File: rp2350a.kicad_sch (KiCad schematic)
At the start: 48 parts, among them Q7 DMN1150UFB-7B, U32 RP2354A, U34 TS2306A 240GF MSM 9_C2976675, U9 TXU0101DCKR, X3 OT4EL89CJI-111YLC-12M

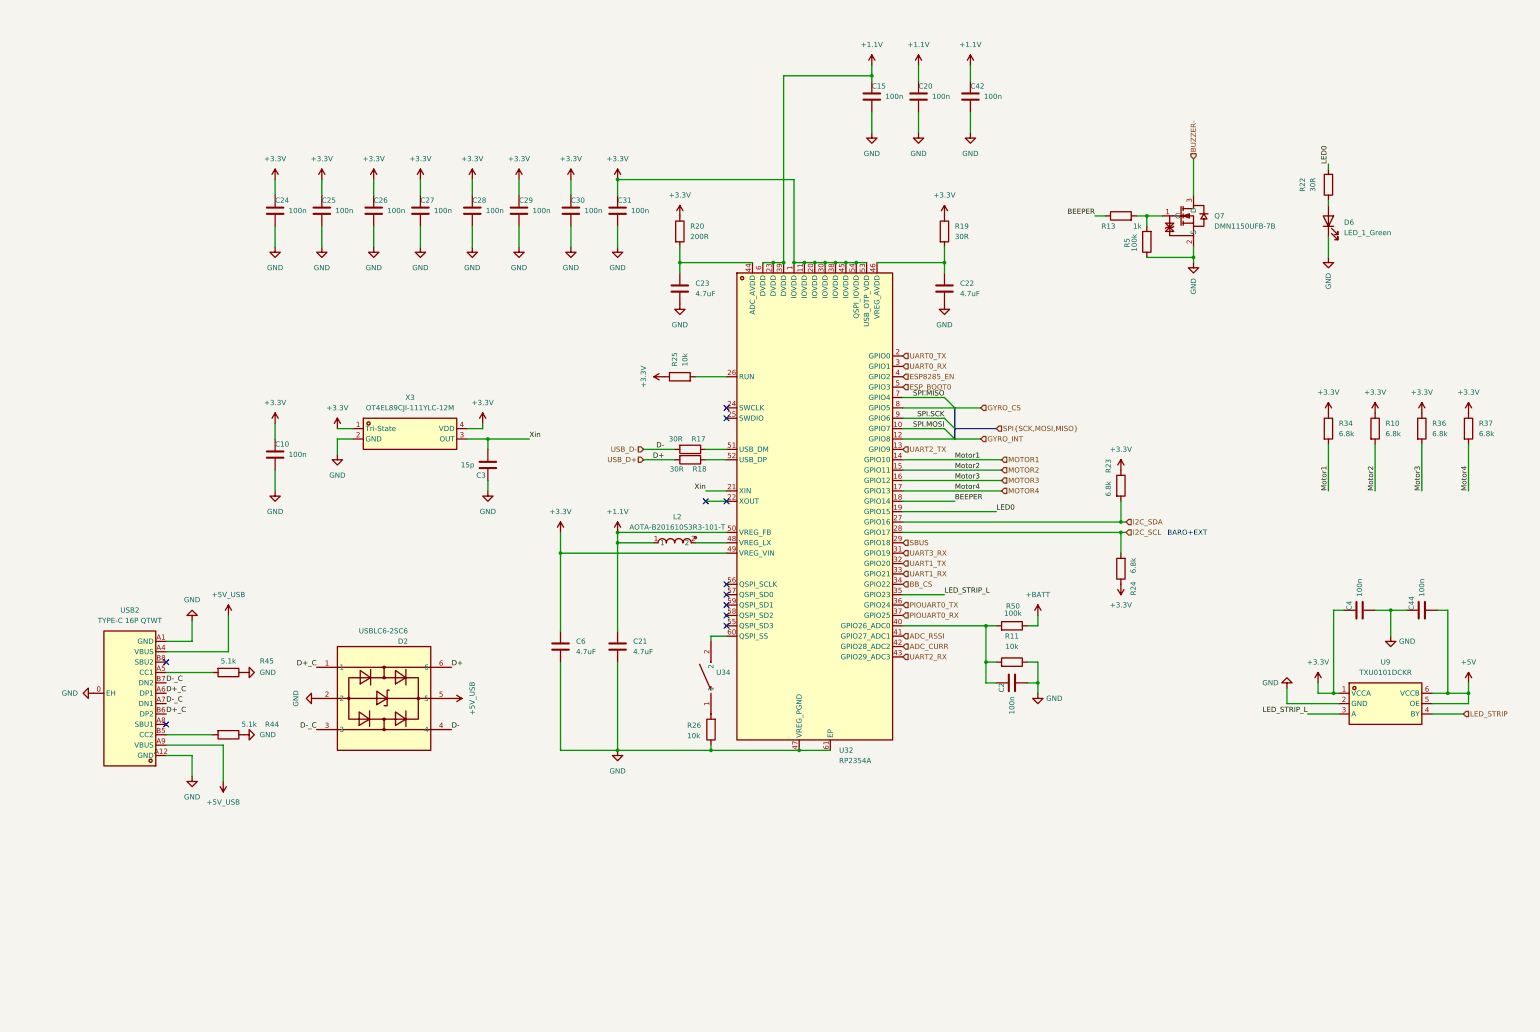
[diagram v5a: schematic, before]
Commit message: Switched to RP2354B for V2 of the FC for more IO. I want to try implement OSD on PIO state machine. I know BF already uses all of them but it should be possible and then later try to combine it witht the WS2812 protocol PIO2. If anybody here has any experience with analog OSD generation let me know, I just want to make a circuit that would allow further software development later. The reason I want to do it this way is it's cheap BOM<1 euro and low footprint, just 2 2x2 IC's and some passives.
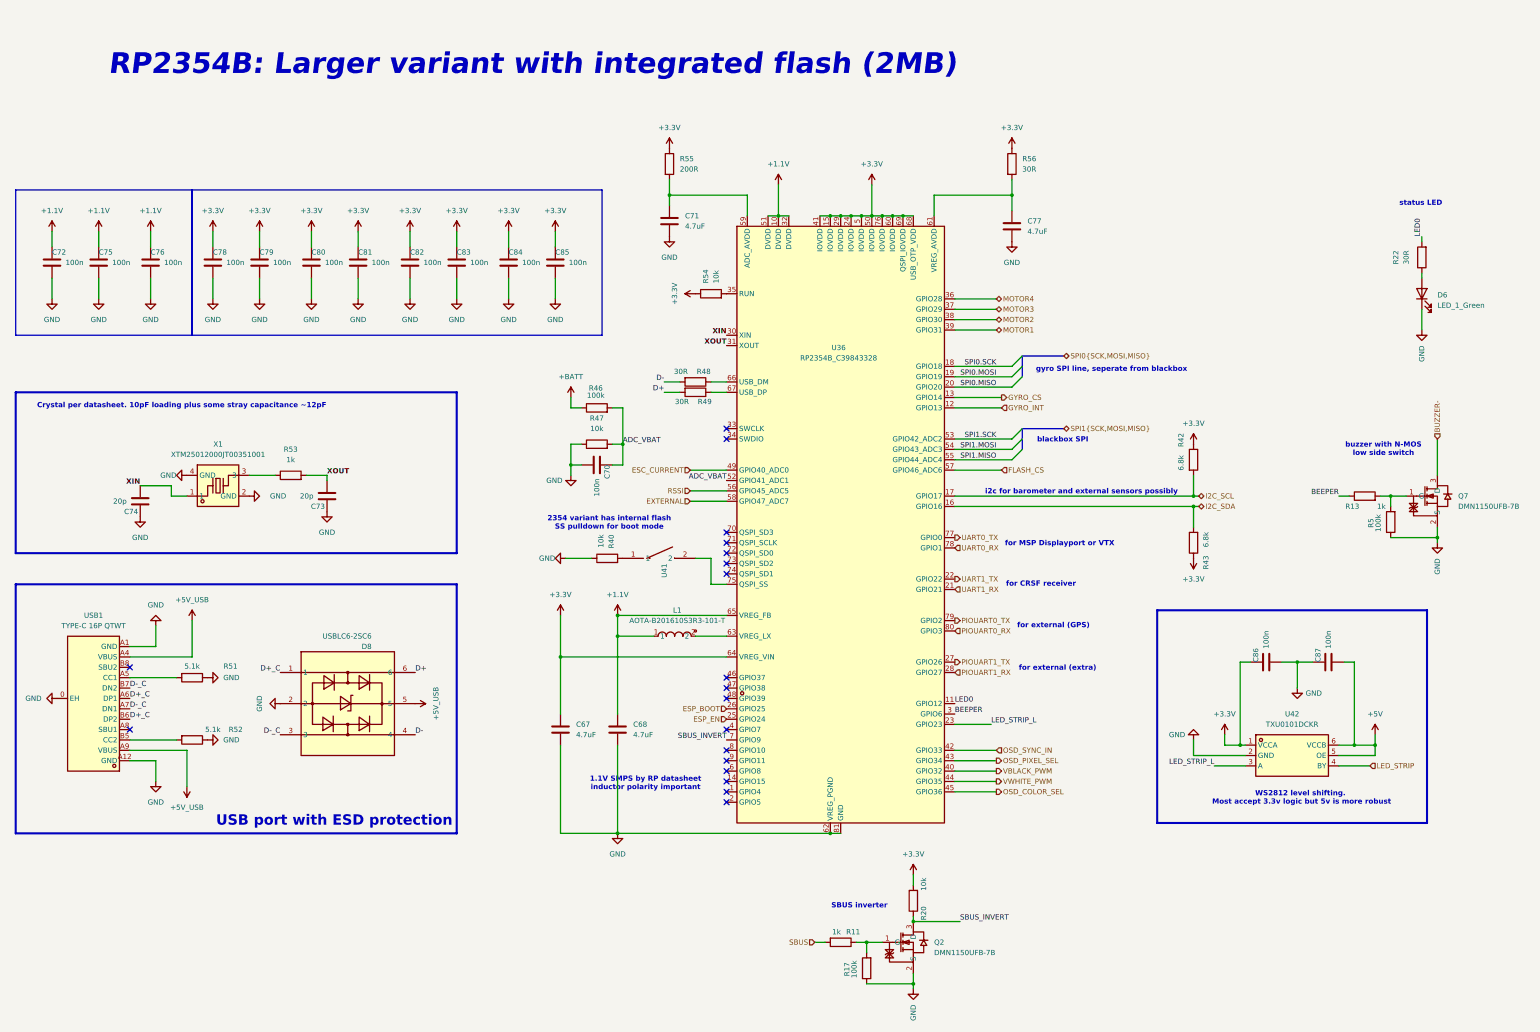
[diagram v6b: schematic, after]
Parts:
- removed C10, C15, C2, C20, C24, C25, C26, C27, C28, C29, C30, C31, C4, C42, C44: 100n, Capacitor_SMD:C_0402_1005Metric, symbol Device:C
- removed C21, C22, C23, C6: 4.7uF, Capacitor_SMD:C_0402_1005Metric, symbol Device:C
- removed C3: 15p, Capacitor_SMD:C_0402_1005Metric, symbol Device:C
- removed D2: USBLC6-2SC6, lib:SOT-23-6_L2.9-W1.6-P0.95-LS2.8-BL, symbol lib:USBLC6-2SC6
- removed L2: AOTA-B201610S3R3-101-T, lib:IND-SMD_L2.0-W1.6_AOTA-B201610S3R3-101-T, symbol lib:AOTA-B201610S3R3-101-T
- removed R10, R23, R24, R34, R36, R37: 6.8k, Resistor_SMD:R_0402_1005Metric, symbol Device:R
- removed R18, R19: 30R, Resistor_SMD:R_0402_1005Metric, symbol Device:R
- removed R25, R26: 10k, Resistor_SMD:R_0402_1005Metric, symbol Device:R
- removed R44, R45: 5.1k, Resistor_SMD:R_0402_1005Metric, symbol Device:R
- removed R50: 100k, Resistor_SMD:R_0402_1005Metric, symbol Device:R
- removed U32: RP2354A, lib:QFN-60_L7.0-W7.0-P0.40-TL-EP3.4, symbol lib:RP2354A
- removed U34: TS2306A 240GF MSM 9_C2976675, lib:SW-SMD_4P-L3.0-W2.0-P0.85-LS3.5, symbol lib:TS2306A240GFMSM9_C2976675
- removed U9: TXU0101DCKR, lib:SC-70-6_L2.0-W1.3-P0.65-LS2.1-BL, symbol lib:TXU0101DCKR
- removed USB2: TYPE-C 16P QTWT, lib:USB-TYPE-C-SMD_TYPE-C-16P-QTWT, symbol lib:TYPE-C16PQTWT
- removed X3: OT4EL89CJI-111YLC-12M, lib:OSC-SMD_4P-L1.6-W1.2-BL-1, symbol lib:OT4EL89CJI-111YLC-12M
- added C67, C68, C71, C77: 4.7uF, Capacitor_SMD:C_0402_1005Metric, symbol Device:C
- added C70, C72, C75, C76, C78, C79, C80, C81, C82, C83, C84, C85, C86, C87: 100n, Capacitor_SMD:C_0402_1005Metric, symbol Device:C
- added C73, C74: 20p, Capacitor_SMD:C_0402_1005Metric, symbol Device:C
- added D8: USBLC6-2SC6, lib:SOT-23-6_L2.9-W1.6-P0.95-LS2.8-BL, symbol lib:USBLC6-2SC6
- added L1: AOTA-B201610S3R3-101-T, lib:IND-SMD_L2.0-W1.6_AOTA-B201610S3R3-101-T, symbol lib:AOTA-B201610S3R3-101-T
- added Q2: DMN1150UFB-7B, lib:DFN-3L_L1.0-W0.6-P0.65-BR, symbol lib:DMN1150UFB-7B
- added R40, R47, R54: 10k, Resistor_SMD:R_0402_1005Metric, symbol Device:R
- added R42, R43: 6.8k, Resistor_SMD:R_0402_1005Metric, symbol Device:R
- added R46: 100k, Resistor_SMD:R_0402_1005Metric, symbol Device:R
- added R48, R49, R56: 30R, Resistor_SMD:R_0402_1005Metric, symbol Device:R
- added R51, R52: 5.1k, Resistor_SMD:R_0402_1005Metric, symbol Device:R
- added R53: 1k, Resistor_SMD:R_0402_1005Metric, symbol Device:R
- added R55: 200R, Resistor_SMD:R_0402_1005Metric, symbol Device:R
- added U36: RP2354B_C39843328, lib:QFN-80_L10.0-W10.0-P0.40-TL-EP3.4, symbol lib:RP2354B_C39843328
- added U41: TS2306A 240GF MSM 9_C2976675, lib:SW-SMD_4P-L3.0-W2.0-P0.85-LS3.5, symbol lib:TS2306A240GFMSM9_C2976675
- added U42: TXU0101DCKR, lib:SC-70-6_L2.0-W1.3-P0.65-LS2.1-BL, symbol lib:TXU0101DCKR
- added USB1: TYPE-C 16P QTWT, lib:USB-TYPE-C-SMD_TYPE-C-16P-QTWT, symbol lib:TYPE-C16PQTWT
- added X1: XTM25012000JT00351001, lib:CRYSTAL-SMD_4P-L2.5-W2.0-BL-A, symbol lib:XTM25012000JT00351001
- R11: value 10k -> 1k; LCSC C2909316 -> C106235
- R17: value 30R -> 100k; LCSC C138007 -> C60491
- R20: value 200R -> 10k; LCSC C25087 -> C106235
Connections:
- net +1.1V: now also C68.1, C72.1, C75.1, C76.1, L1.1, U36.10 (DVDD), U36.32 (DVDD), U36.51 (DVDD), U36.65 (VREG_FB)
- net +3.3V: now also R20.2, C67.1, C78.1, C79.1, C80.1, C81.1, C82.1, C83.1, C84.1, C85.1, C86.1, R42.1, R43.1, R54.1, R55.1, R56.1, U36.15 (IOVDD), U36.24 (IOVDD), U36.29 (IOVDD), U36.41 (IOVDD), U36.5 (IOVDD), U36.50 (IOVDD), U36.60 (IOVDD), U36.64 (VREG_VIN), U36.68 (USB_OTP_VDD), U36.69 (QSPI_IOVDD), U36.76 (IOVDD), U42.1 (VCCA); no longer R20.1
- net +5V: now also C87.2, U42.5 (OE), U42.6 (VCCB)
- net +5V_USB: now also D8.5, USB1.A4 (VBUS), USB1.A9 (VBUS)
- net +BATT: now also R46.1
- net BEEPER: now also U36.3 (GPIO6)
- net D+_C: now also D8.1, USB1.A6 (DP1), USB1.B6 (DP2)
- net D-_C: now also D8.3, USB1.A7 (DN1), USB1.B7 (DN2)
- net GND: now also R17.1, C67.2, C68.2, C70.2, C71.2, C72.2, C73.1, C74.1, C75.2, C76.2, C77.2, C78.2, C79.2, C80.2, C81.2, C82.2, C83.2, C84.2, C85.2, C86.2, C87.1, D8.2, Q2.2 (S), R40.1, R47.1, R51.1, R52.1, U36.62 (VREG_PGND), U36.81 (GND), U42.2 (GND), USB1.0 (EH), USB1.A1 (GND), USB1.A12 (GND), X1.2 (GND), X1.4 (GND); no longer R11.1
- net GYRO_CS: now also U36.13 (GPIO14)
- net GYRO_INT: now also U36.12 (GPIO13)
- net I2C_SCL: now also R42.2, U36.17 (GPIO17)
- net I2C_SDA: now also R43.2, U36.16 (GPIO16)
- net LED0: now also U36.11 (GPIO12)
- net LED_STRIP: now also U42.4 (BY)
- net LED_STRIP_L: now also U36.23 (GPIO23), U42.3 (A)
- net MOTOR1: now also U36.39 (GPIO31)
- net MOTOR2: now also U36.38 (GPIO30)
- net MOTOR3: now also U36.37 (GPIO29)
- net MOTOR4: now also U36.36 (GPIO28)
- net PIOUART0_RX: now also U36.80 (GPIO3)
- net PIOUART0_TX: now also U36.79 (GPIO2)
- net SBUS: now also R11.2
- net UART0_RX: now also U36.78 (GPIO1)
- net UART0_TX: now also U36.77 (GPIO0)
- net UART1_RX: now also U36.21 (GPIO21)
- net UART1_TX: now also U36.22 (GPIO22)
- net USB_D-: no longer names the net of R17.2
- net USB_D-: now also R11.1, Q2.1 (G)
- new net: R40.2, U41.1
- new net: U36.75 (QSPI_SS), U41.2
- new net: R49.1, U36.67 (USB_DP)
- new net: R51.2, USB1.A5 (CC1)
- new net: R52.2, USB1.B5 (CC2)
- new net: R54.2, U36.35 (RUN)
- new net: R53.1, X1.3
- new net: C77.1, R56.2, U36.61 (VREG_AVDD)
- new net: C71.1, R55.2, U36.59 (ADC_AVDD)
- new net: L1.2, U36.63 (VREG_LX)
- new net: R48.1, U36.66 (USB_DM)
- new net ADC_VBAT: C70.1, R46.2, R47.2, U36.52 (GPIO41_ADC1)
- new net D+: D8.6, R49.2
- new net D-: D8.4, R48.2
- new net ESC_CURRENT: U36.49 (GPIO40_ADC0)
- new net ESP_BOOT: U36.26 (GPIO25)
- new net ESP_EN: U36.25 (GPIO24)
- new net EXTERNAL: U36.58 (GPIO47_ADC7)
- new net FLASH_CS: U36.57 (GPIO46_ADC6)
- new net OSD_COLOR_SEL: U36.45 (GPIO36)
- new net OSD_PIXEL_SEL: U36.43 (GPIO34)
- new net OSD_SYNC_IN: U36.42 (GPIO33)
- new net PIOUART1_RX: U36.28 (GPIO27)
- new net PIOUART1_TX: U36.27 (GPIO26)
- new net RSSI: U36.56 (GPIO45_ADC5)
- new net SBUS_INVERT: Q2.3 (D), R20.1, U36.7 (GPIO9)
- new net SPI0.MISO: U36.20 (GPIO20)
- new net SPI0.MOSI: U36.19 (GPIO19)
- new net SPI0.SCK: U36.18 (GPIO18)
- new net SPI1.MISO: U36.55 (GPIO44_ADC4)
- new net SPI1.MOSI: U36.54 (GPIO43_ADC3)
- new net SPI1.SCK: U36.53 (GPIO42_ADC2)
- new net VBLACK_PWM: U36.40 (GPIO32)
- new net VWHITE_PWM: U36.44 (GPIO35)
- new net XIN: C74.2, U36.30 (XIN), X1.1
- new net XOUT: C73.2, R53.2, U36.31 (XOUT)
- no-connect marks 11 -> 19
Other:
- note added: "1.1V SMPS by RP datasheet inductor polarity important"
- note added: "2354 variant has internal flash SS pulldown for boot mode"
- note added: "Crystal per datasheet. 10pF loading plus some stray capacitance ~12pF"
- note added: "RP2354B: Larger variant with integrated flash (2MB)"
- note added: "SBUS inverter"
- note added: "USB port with ESD protection"
- note added: "WS2812 level shifting. Most accept 3.3v logic but 5v is more robust"
- note added: "blackbox SPI"
- note added: "buzzer with N-MOS low side switch"
- note added: "for CRSF receiver"
- note added: "for MSP Displayport or VTX"
- note added: "for external (GPS)"
- note added: "for external (extra)"
- note added: "gyro SPI line, seperate from blackbox"
- note added: "i2c for barometer and external sensors possibly"
- note added: "status LED"
- note removed: "BARO+EXT"
- moved on the sheet: D6, Q7, R13, R22, R5
